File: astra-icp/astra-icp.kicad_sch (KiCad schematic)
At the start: 71 parts, among them IC1 ATA6561-GAQW-N, J1 SWD, J2 PWR_IN, J3 CAN_TERMINAL, J4 UART, SW1 CHOC_HS, SW10 CHOC_HS, SW11 CHOC_HS, SW12 CHOC_HS, SW13 CHOC_HS, SW14 CHOC_HS, SW15 CHOC_HS, SW16 CHOC_HS, SW17 CHOC_HS, SW18 CHOC_HS, SW19 CHOC_HS, SW2 CHOC_HS, SW20 CHOC_HS, SW3 CHOC_HS, SW4 CHOC_HS, SW5 CHOC_HS, SW6 CHOC_HS, SW7 CHOC_HS, SW8 CHOC_HS, SW9 CHOC_HS, U3 STM32F042C4Tx

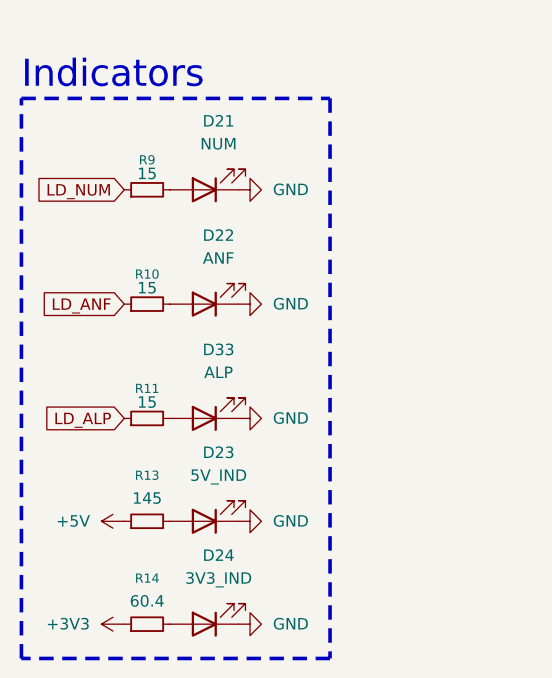
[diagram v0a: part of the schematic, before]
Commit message: fix: Corrected resistor values for LEDs
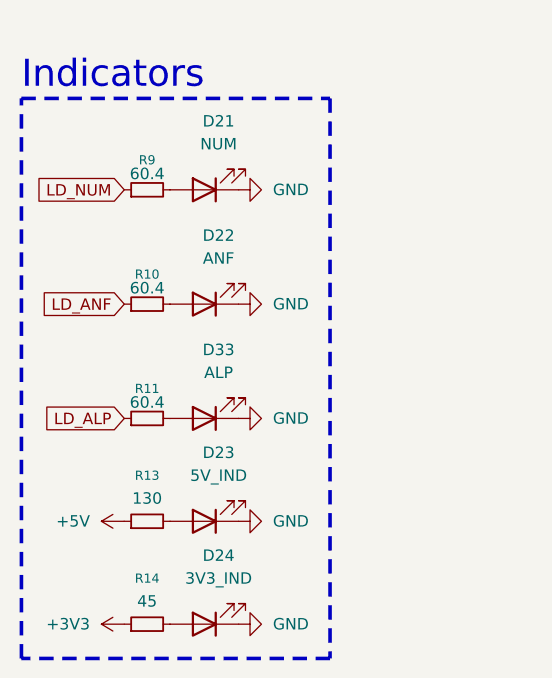
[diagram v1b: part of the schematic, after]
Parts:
- R10, R11, R9: value 15 -> 60.4
- R13: value 145 -> 130
- R14: value 60.4 -> 45
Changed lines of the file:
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@@
 			)
 		)
-		(property "Value" "15"
+		(property "Value" "60.4"
 			(at 39.37 160.782 90)
 			(effects
@@
 			)
 		)
-		(property "Value" "145"
+		(property "Value" "130"
 			(at 39.37 171.45 90)
 			(effects
@@
 			)
 		)
-		(property "Value" "15"
+		(property "Value" "60.4"
 			(at 39.37 135.382 90)
 			(effects
@@
 			)
 		)
-		(property "Value" "15"
+		(property "Value" "60.4"
 			(at 39.37 148.082 90)
 			(effects
@@
 			)
 		)
-		(property "Value" "60.4"
+		(property "Value" "45"
 			(at 39.37 182.88 90)
 			(effects

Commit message: fix: More tweaks for real component choice
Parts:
- D1: footprint PCM_Diode_SMD_AKL:D_0603_1608Metric_Pad1.05x0.95mm_HandSolder -> Diode_SMD:D_SOD-323; Part Number (none) -> BAV16WS-7-F
- D10, D11, D12, D13, D14, D15, D16, D17, D18, D19, D2, D20, D3, D4, D5, D6, D7, D8, D9: footprint PCM_Diode_SMD_AKL:D_0603_1608Metric_Pad1.05x0.95mm_HandSolder -> Diode_SMD:D_SOD-323
- R14: value 45 -> 47
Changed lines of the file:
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@@
 			)
 		)
-		(property "Footprint" "PCM_Diode_SMD_AKL:D_0603_1608Metric_Pad1.05x0.95mm_HandSolder"
+		(property "Footprint" "Diode_SMD:D_SOD-323"
 			(at 121.92 50.8 90)
 			(effects
@@
 			)
 		)
-		(property "Footprint" "PCM_Diode_SMD_AKL:D_0603_1608Metric_Pad1.05x0.95mm_HandSolder"
+		(property "Footprint" "Diode_SMD:D_SOD-323"
 			(at 45.72 50.8 90)
 			(effects
@@
 			)
 		)
-		(property "Footprint" "PCM_Diode_SMD_AKL:D_0603_1608Metric_Pad1.05x0.95mm_HandSolder"
+		(property "Footprint" "Diode_SMD:D_SOD-323"
 			(at 83.82 50.8 90)
 			(effects
@@
 			)
 		)
-		(property "Footprint" "PCM_Diode_SMD_AKL:D_0603_1608Metric_Pad1.05x0.95mm_HandSolder"
+		(property "Footprint" "Diode_SMD:D_SOD-323"
 			(at 58.42 63.5 90)
 			(effects
@@
 			)
 		)
-		(property "Footprint" "PCM_Diode_SMD_AKL:D_0603_1608Metric_Pad1.05x0.95mm_HandSolder"
+		(property "Footprint" "Diode_SMD:D_SOD-323"
 			(at 71.12 38.1 90)
 			(effects
@@
 			)
 		)
-		(property "Footprint" "PCM_Diode_SMD_AKL:D_0603_1608Metric_Pad1.05x0.95mm_HandSolder"
+		(property "Footprint" "Diode_SMD:D_SOD-323"
 			(at 71.12 50.8 90)
 			(effects
@@
 			)
 		)
-		(property "Footprint" "PCM_Diode_SMD_AKL:D_0603_1608Metric_Pad1.05x0.95mm_HandSolder"
+		(property "Footprint" "Diode_SMD:D_SOD-323"
 			(at 134.62 38.1 90)
 			(effects
@@
 			)
 		)
-		(property "Footprint" "PCM_Diode_SMD_AKL:D_0603_1608Metric_Pad1.05x0.95mm_HandSolder"
+		(property "Footprint" "Diode_SMD:D_SOD-323"
 			(at 109.22 41.91 90)
 			(effects
@@
 			)
 		)
-		(property "Footprint" "PCM_Diode_SMD_AKL:D_0603_1608Metric_Pad1.05x0.95mm_HandSolder"
+		(property "Footprint" "Diode_SMD:D_SOD-323"
 			(at 121.92 63.5 90)
 			(effects
@@
 			)
 		)
-		(property "Footprint" "PCM_Diode_SMD_AKL:D_0603_1608Metric_Pad1.05x0.95mm_HandSolder"
+		(property "Footprint" "Diode_SMD:D_SOD-323"
 			(at 134.62 50.8 90)
 			(effects
@@
 			)
 		)
-		(property "Footprint" "PCM_Diode_SMD_AKL:D_0603_1608Metric_Pad1.05x0.95mm_HandSolder"
+		(property "Footprint" "Diode_SMD:D_SOD-323"
 			(at 45.72 63.5 90)
 			(effects
@@
 			)
 		)
-		(property "Footprint" "PCM_Diode_SMD_AKL:D_0603_1608Metric_Pad1.05x0.95mm_HandSolder"
+		(property "Footprint" "Diode_SMD:D_SOD-323"
 			(at 134.62 63.5 90)
 			(effects
@@
 			)
 		)
-		(property "Footprint" "PCM_Diode_SMD_AKL:D_0603_1608Metric_Pad1.05x0.95mm_HandSolder"
+		(property "Footprint" "Diode_SMD:D_SOD-323"
 			(at 71.12 63.5 90)
 			(effects
@@
 			)
 		)
-		(property "Footprint" "PCM_Diode_SMD_AKL:D_0603_1608Metric_Pad1.05x0.95mm_HandSolder"
+		(property "Footprint" "Diode_SMD:D_SOD-323"
 			(at 83.82 38.1 90)
 			(effects
@@
 			)
 		)
-		(property "Footprint" "PCM_Diode_SMD_AKL:D_0603_1608Metric_Pad1.05x0.95mm_HandSolder"
+		(property "Footprint" "Diode_SMD:D_SOD-323"
 			(at 96.52 38.1 90)
 			(effects
@@
 			)
 		)
-		(property "Footprint" "PCM_Diode_SMD_AKL:D_0603_1608Metric_Pad1.05x0.95mm_HandSolder"
+		(property "Footprint" "Diode_SMD:D_SOD-323"
 			(at 83.82 63.5 90)
 			(effects
@@
 			)
 		)
-		(property "Footprint" "PCM_Diode_SMD_AKL:D_0603_1608Metric_Pad1.05x0.95mm_HandSolder"
+		(property "Footprint" "Diode_SMD:D_SOD-323"
 			(at 45.72 38.1 90)
 			(effects
@@
 			)
 		)
+		(property "Part Number" "BAV16WS-7-F "
+			(at 45.72 38.1 0)
+			(effects
+				(font
+					(size 1.27 1.27)
+				)
+				(hide yes)
+			)
+		)
 		(pin "1"
 		)
@@
 			)
 		)
-		(property "Footprint" "PCM_Diode_SMD_AKL:D_0603_1608Metric_Pad1.05x0.95mm_HandSolder"
+		(property "Footprint" "Diode_SMD:D_SOD-323"
 			(at 121.92 38.1 90)
 			(effects
@@
 			)
 		)
-		(property "Footprint" "PCM_Diode_SMD_AKL:D_0603_1608Metric_Pad1.05x0.95mm_HandSolder"
+		(property "Footprint" "Diode_SMD:D_SOD-323"
 			(at 58.42 38.1 90)
 			(effects
@@
 			)
 		)
-		(property "Value" "45"
+		(property "Value" "47"
 			(at 39.37 182.88 90)
 			(effects
@@
 			)
 		)
-		(property "Footprint" "PCM_Diode_SMD_AKL:D_0603_1608Metric_Pad1.05x0.95mm_HandSolder"
+		(property "Footprint" "Diode_SMD:D_SOD-323"
 			(at 58.42 50.8 90)
 			(effects

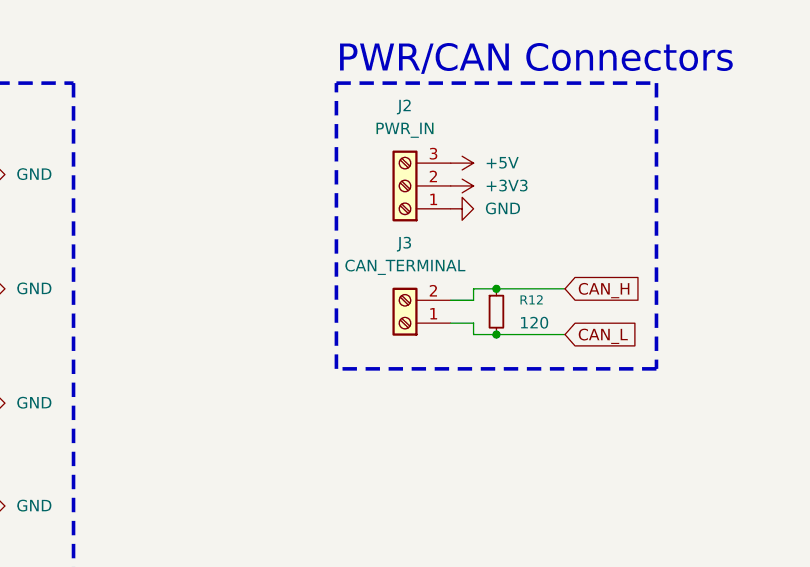
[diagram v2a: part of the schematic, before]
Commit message: Changed CAN connector in ICP
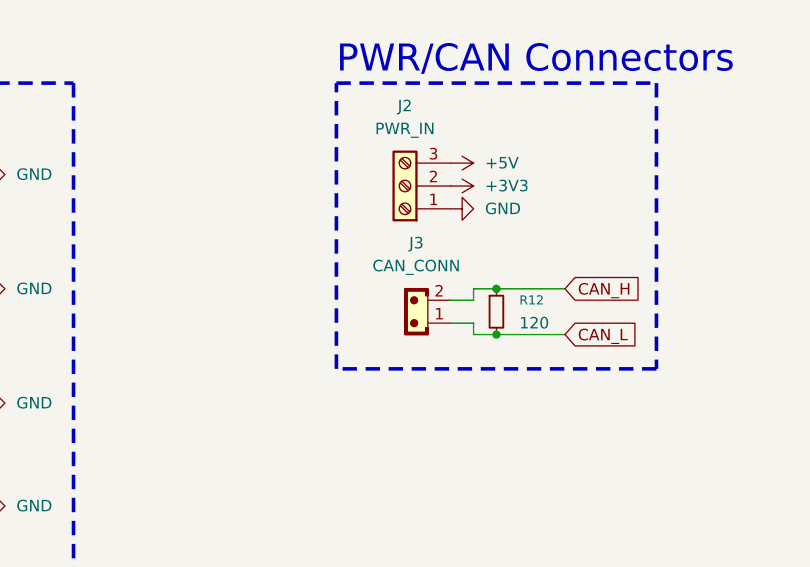
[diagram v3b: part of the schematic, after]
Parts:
- removed J3: CAN_TERMINAL, TerminalBlock_Phoenix:TerminalBlock_Phoenix_PT-1,5-2-5.0-H_1x02_P5.00mm_Horizontal, symbol Connector:Screw_Terminal_01x02
- added J3: CAN_CONN, Connector_JST:JST_PH_B2B-PH-K_1x02_P2.00mm_Vertical, symbol PCM_SL_Connectors:JST_02
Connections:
- net CAN_H: now also J3.2
- net CAN_L: now also J3.1

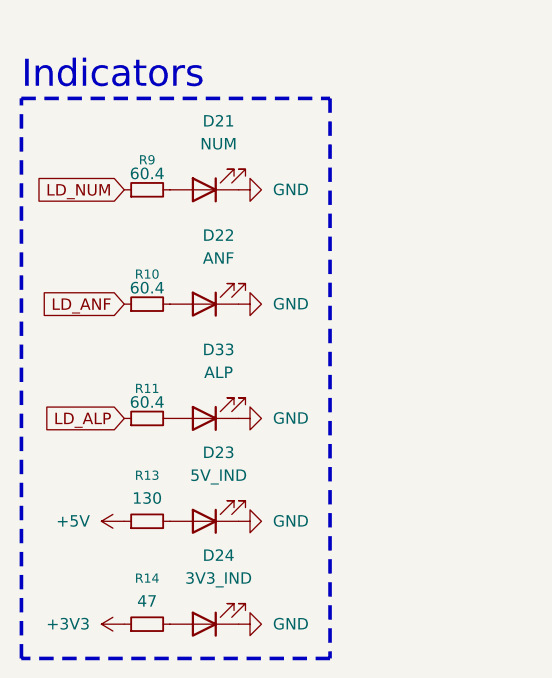
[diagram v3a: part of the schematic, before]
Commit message: Minor tweaks to schematics HAT and ICP
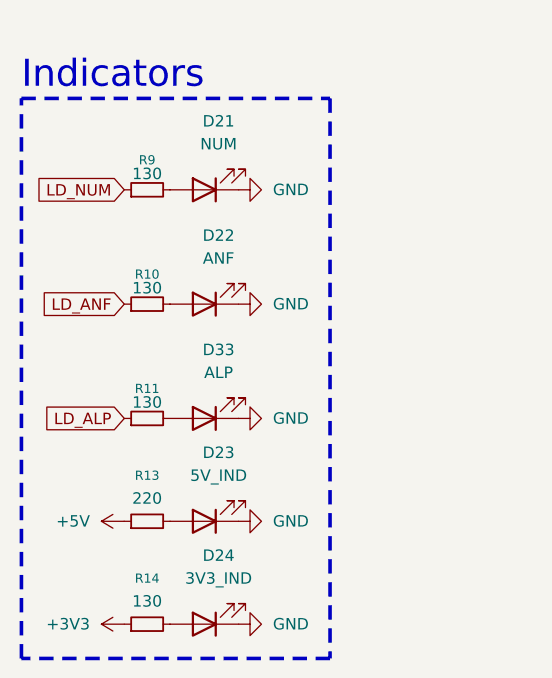
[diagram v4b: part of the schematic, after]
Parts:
- R10, R11, R9: value 60.4 -> 130
- R13: value 130 -> 220
- R14: value 47 -> 130
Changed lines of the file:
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@@
 			)
 		)
-		(property "Value" "60.4"
+		(property "Value" "130"
 			(at 39.37 160.782 90)
 			(show_name no)
@@
 			)
 		)
-		(property "Value" "130"
+		(property "Value" "220"
 			(at 39.37 171.45 90)
 			(show_name no)
@@
 			)
 		)
-		(property "Value" "60.4"
+		(property "Value" "130"
 			(at 39.37 135.382 90)
 			(show_name no)
@@
 			)
 		)
-		(property "Value" "60.4"
+		(property "Value" "130"
 			(at 39.37 148.082 90)
 			(show_name no)
@@
 			)
 		)
-		(property "Value" "47"
+		(property "Value" "130"
 			(at 39.37 182.88 90)
 			(show_name no)
